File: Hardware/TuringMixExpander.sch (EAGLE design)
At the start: 35 parts, among them IC1 TL074P, IC2 TL072P

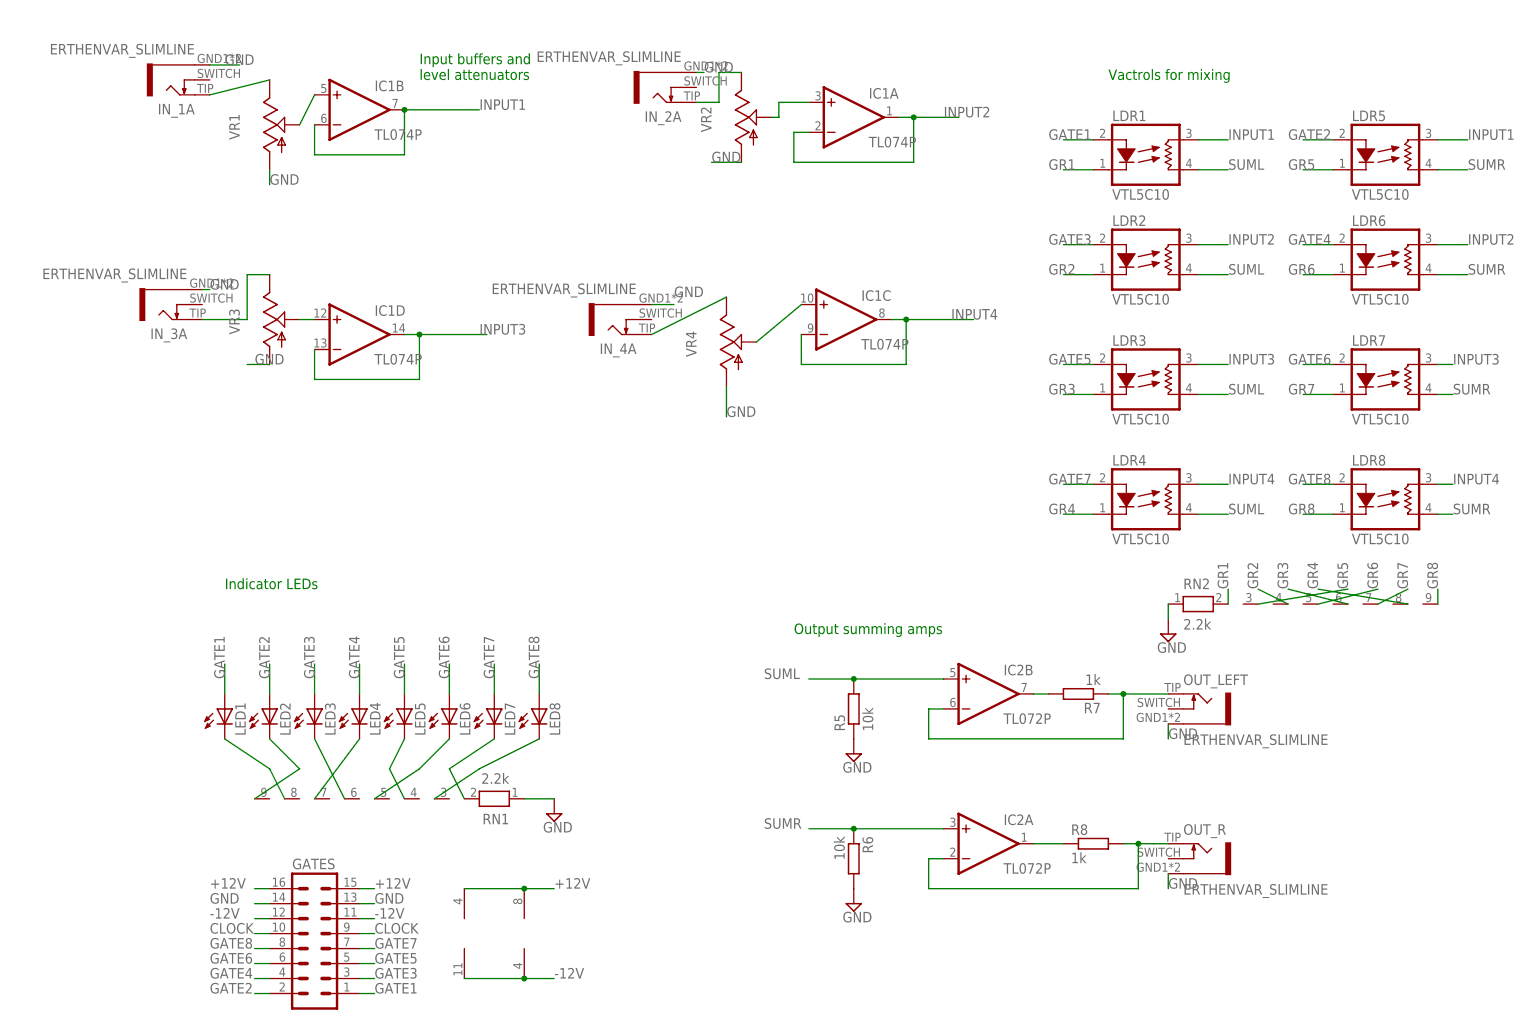
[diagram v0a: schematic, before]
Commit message: New pcb layout
Added passthrough header
Removed resistor networks
Simplified led/resistor structure (one per channel, not two)
New panel layout
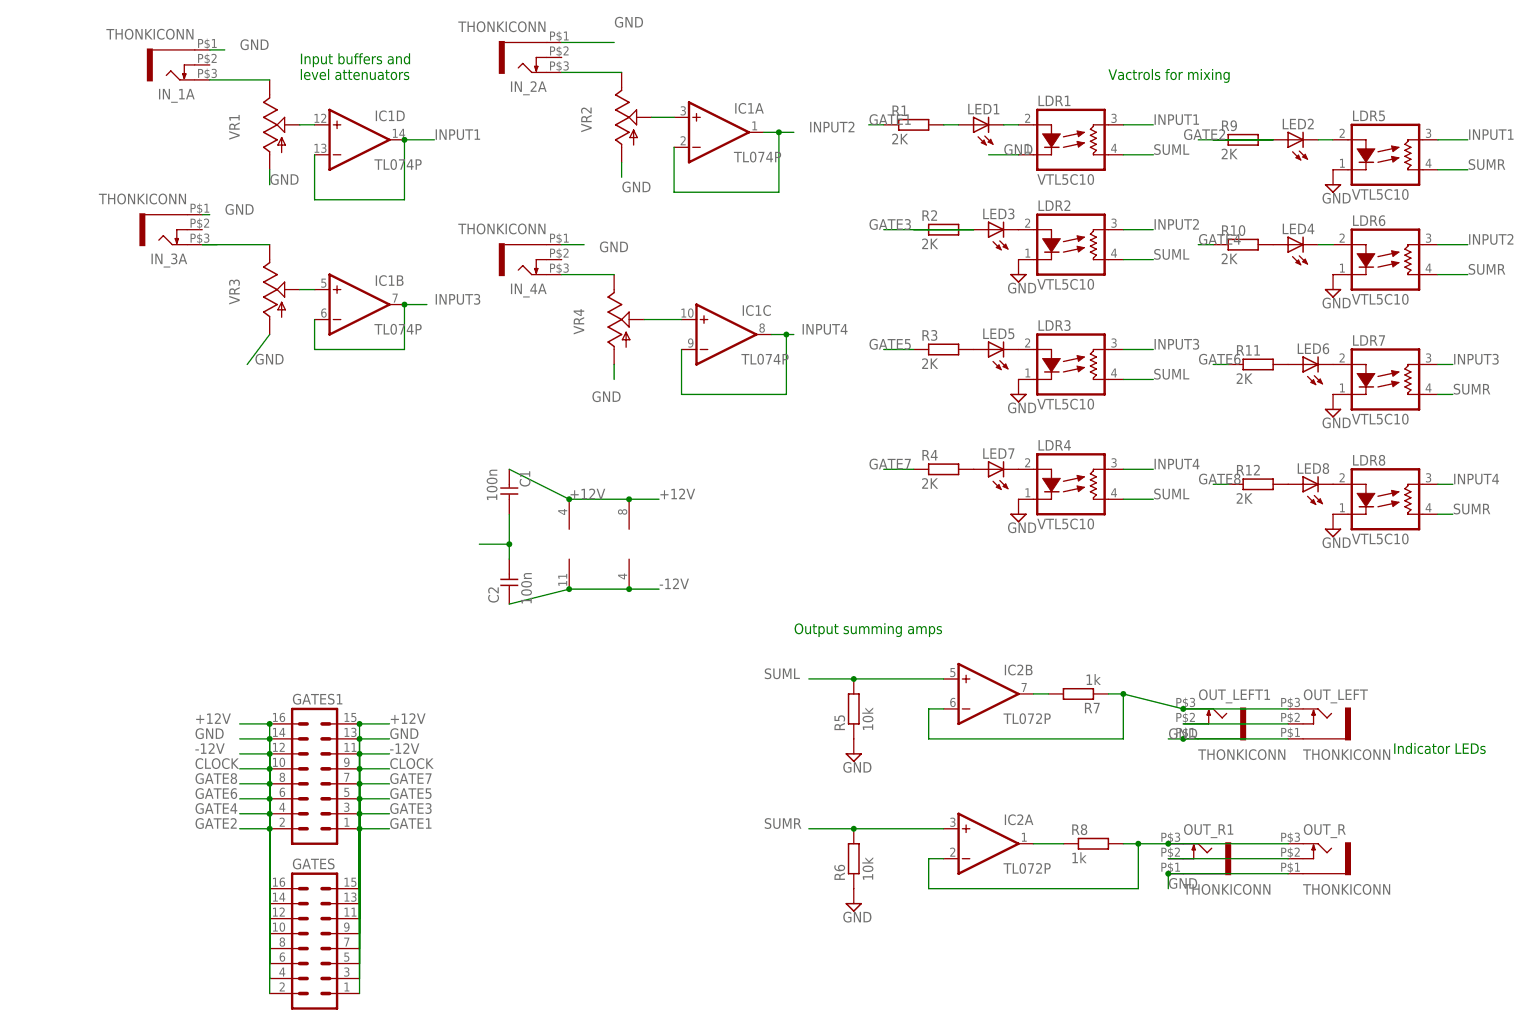
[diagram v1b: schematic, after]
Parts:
- removed RN1, RN2: 2.2k, resistor-net:RN08
- added C1, C2: 100n, TomW:C-EU050-024X044
- added GATES1: (no value), con-lstb:MA08-2
- added OUT_LEFT1, OUT_R1: THONKICONN, TomW:THONKICONN
- added R1, R10, R11, R12, R2, R3, R4, R9: 2K, TomW:R-EU_0207/10
- IN_1A, IN_2A, IN_3A, IN_4A, OUT_LEFT, OUT_R: value ERTHENVAR_SLIMLINE -> THONKICONN; device TomW:ERTHENVAR_SLIMLINE -> TomW:THONKICONN
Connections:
- removed net GR1: LDR1.C, RN2.2
- removed net GR2: LDR2.C, RN2.4
- removed net GR3: LDR3.C, RN2.6
- removed net GR4: LDR4.C, RN2.8
- removed net GR5: LDR5.C, RN2.3
- removed net GR6: LDR6.C, RN2.5
- removed net GR7: LDR7.C, RN2.7
- removed net GR8: LDR8.C, RN2.9
- new net N$14: LDR1.A, LED1.C
- new net N$24: OUT_R.4, OUT_R1.4
- new net N$25: LED1.A, R1.2
- new net N$26: LED3.A, R2.1
- new net N$27: LED5.A, R3.2
- new net N$28: LED7.A, R4.2
- new net N$29: LED2.A, R9.1
- new net N$30: LED4.A, R10.2
- new net N$31: LED6.A, R11.2
- new net N$32: LED8.A, R12.2
- net +12V: now also C1.2, GATES1.15, GATES1.16
- net -12V: now also C2.2, GATES1.11, GATES1.12
- net CLOCK: now also GATES1.10, GATES1.9
- net GATE1: now also GATES1.1, R1.1; no longer LDR1.A, LED1.A
- net GATE2: now also GATES1.2, R9.2; no longer LDR5.A, LED2.A
- net GATE3: now also GATES1.3, R2.2; no longer LDR2.A, LED3.A
- net GATE4: now also GATES1.4, R10.1; no longer LDR6.A, LED4.A
- net GATE5: now also GATES1.5, R3.1; no longer LDR3.A, LED5.A
- net GATE6: now also GATES1.6, R11.1; no longer LDR7.A, LED6.A
- net GATE7: now also GATES1.7, R4.1; no longer LDR4.A, LED7.A
- net GATE8: now also GATES1.8, R12.1; no longer LDR8.A, LED8.A
- net GND: now also C1.1, C2.1, GATES1.13, GATES1.14, LDR1.C, LDR2.C, LDR3.C, LDR4.C, LDR5.C, LDR6.C, LDR7.C, LDR8.C, OUT_LEFT1.5, OUT_R1.5, R6.1; no longer R6.2, RN1.1, RN2.1
- net INPUT1: now also IC1D.-IN, IC1D.OUT; no longer IC1B.-IN, IC1B.OUT
- net INPUT3: now also IC1B.-IN, IC1B.OUT; no longer IC1D.-IN, IC1D.OUT
- net N$10: now also OUT_R1.3
- net N$11: now also IC1B.+IN; no longer IC1D.+IN
- net N$15: now also LDR2.A, LED3.C; no longer LED1.C, RN1.8
- net N$16: now also LDR3.A, LED5.C; no longer LED2.C, RN1.9
- net N$17: now also LDR4.A, LED7.C; no longer LED3.C, RN1.6
- net N$18: now also LDR5.A, LED2.C; no longer LED4.C, RN1.7
- net N$19: now also LDR6.A, LED4.C; no longer LED5.C, RN1.4
- net N$2: now also IC1D.+IN; no longer IC1B.+IN
- net N$20: now also LDR7.A; no longer RN1.5
- net N$21: now also LDR8.A, LED8.C; no longer LED7.C, RN1.2
- net N$22: now also OUT_LEFT.4, OUT_LEFT1.4; no longer LED8.C, RN1.3
- net N$7: now also OUT_LEFT1.3
- net SUMR: now also R6.2; no longer R6.1
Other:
- moved on the sheet: IC1A, IC1B, IC1C, IC1D, IN_1A, IN_2A, IN_3A, IN_4A, LDR1, LDR2, LDR3, LDR4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

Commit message: New resistor grid
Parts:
- R1, R10, R11, R12, R2, R3, R4, R5, R6, R7, R8, R9: device TomW:R-EU_0207/10 -> TomW:R-EU_0207/7
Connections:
- net GATE1: now also R1.2; no longer R1.1
- net GND: now also LDR1.LED-, LDR2.LED-, LDR3.LED-, LDR4.LED-, LDR5.LED-, LDR6.LED-, LDR7.LED-, LDR8.LED-; no longer LDR1.C, LDR2.C, LDR3.C, LDR4.C, LDR5.C, LDR6.C, LDR7.C, LDR8.C
- net INPUT1: now also LDR1.RES1, LDR5.RES1; no longer LDR1.L1, LDR5.L1
- net INPUT2: now also LDR2.RES1, LDR6.RES1; no longer LDR2.L1, LDR6.L1
- net INPUT3: now also LDR3.RES1, LDR7.RES1; no longer LDR3.L1, LDR7.L1
- net INPUT4: now also LDR4.RES1, LDR8.RES1; no longer LDR4.L1, LDR8.L1
- net N$14: now also LDR1.LED+; no longer LDR1.A
- net N$15: now also LDR2.LED+; no longer LDR2.A
- net N$16: now also LDR3.LED+; no longer LDR3.A
- net N$17: now also LDR4.LED+; no longer LDR4.A
- net N$18: now also LDR5.LED+; no longer LDR5.A
- net N$19: now also LDR6.LED+; no longer LDR6.A
- net N$20: now also LDR7.LED+; no longer LDR7.A
- net N$21: now also LDR8.LED+; no longer LDR8.A
- net N$25: now also R1.1; no longer R1.2
- net SUML: now also LDR1.RES2, LDR2.RES2, LDR3.RES2, LDR4.RES2; no longer LDR1.L2, LDR2.L2, LDR3.L2, LDR4.L2
- net SUMR: now also LDR5.RES2, LDR6.RES2, LDR7.RES2, LDR8.RES2; no longer LDR5.L2, LDR6.L2, LDR7.L2, LDR8.L2

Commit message: PCB work
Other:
- moved on the sheet: IN_3A, LED3, R1, R2, R9
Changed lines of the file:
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@@
 <instance part="IN_1A" gate="G$1" x="17.78" y="167.64" rot="R180"/>
 <instance part="IN_2A" gate="G$1" x="77.47" y="168.91" rot="R180"/>
-<instance part="IN_3A" gate="G$1" x="16.51" y="139.7" rot="R180"/>
+<instance part="IN_3A" gate="G$1" x="13.97" y="139.7" rot="R180"/>
 <instance part="IN_4A" gate="G$1" x="77.47" y="134.62" rot="R180"/>
 <instance part="IC1" gate="D" x="48.26" y="154.94"/>
@@
 <instance part="LED1" gate="G$1" x="152.4" y="157.48" rot="R90"/>
 <instance part="LED2" gate="G$1" x="205.74" y="154.94" rot="R90"/>
-<instance part="LED3" gate="G$1" x="154.94" y="139.7" rot="R90"/>
+<instance part="LED3" gate="G$1" x="152.4" y="139.7" rot="R90"/>
 <instance part="LED4" gate="G$1" x="205.74" y="137.16" rot="R90"/>
 <instance part="LED5" gate="G$1" x="154.94" y="119.38" rot="R90"/>
@@
 <instance part="FRAME1" gate="G$1" x="0" y="0"/>
 <instance part="GATES1" gate="G$1" x="40.64" y="45.72"/>
-<instance part="R1" gate="G$1" x="142.24" y="157.48"/>
+<instance part="R1" gate="G$1" x="142.24" y="157.48" rot="R180"/>
 <instance part="C1" gate="G$1" x="73.66" y="93.98" rot="R180"/>
 <instance part="C2" gate="G$1" x="73.66" y="81.28"/>
@@
 <instance part="SUPPLY8" gate="GND" x="213.36" y="129.54"/>
 <instance part="SUPPLY9" gate="GND" x="213.36" y="147.32"/>
-<instance part="R2" gate="G$1" x="147.32" y="139.7"/>
+<instance part="R2" gate="G$1" x="142.24" y="139.7" rot="R180"/>
 <instance part="R3" gate="G$1" x="147.32" y="119.38"/>
 <instance part="R4" gate="G$1" x="147.32" y="99.06"/>
-<instance part="R9" gate="G$1" x="198.12" y="154.94"/>
+<instance part="R9" gate="G$1" x="198.12" y="154.94" rot="R180"/>
 <instance part="R10" gate="G$1" x="198.12" y="137.16"/>
 <instance part="R11" gate="G$1" x="200.66" y="116.84"/>
@@
 <segment>
 <pinref part="IN_3A" gate="G$1" pin="5"/>
-<wire x1="22.86" y1="142.24" x2="21.59" y2="142.24" width="0.1524" layer="91"/>
+<wire x1="22.86" y1="142.24" x2="19.05" y2="142.24" width="0.1524" layer="91"/>
 <label x="25.4" y="142.24" size="1.778" layer="95"/>
 </segment>
@@
 <wire x1="68.58" y1="86.36" x2="73.66" y2="86.36" width="0.1524" layer="91"/>
 <junction x="73.66" y="86.36"/>
+<label x="66.04" y="86.36" size="1.778" layer="95" rot="R180"/>
 </segment>
 <segment>
@@
 <segment>
 <pinref part="R1" gate="G$1" pin="2"/>
-<wire x1="134.62" y1="157.48" x2="147.32" y2="157.48" width="0.1524" layer="91"/>
+<wire x1="134.62" y1="157.48" x2="137.16" y2="157.48" width="0.1524" layer="91"/>
 <label x="134.62" y="157.48" size="1.778" layer="95"/>
 </segment>
@@
 <segment>
 <pinref part="R9" gate="G$1" pin="2"/>
-<wire x1="190.5" y1="154.94" x2="203.2" y2="154.94" width="0.1524" layer="91"/>
+<wire x1="190.5" y1="154.94" x2="193.04" y2="154.94" width="0.1524" layer="91"/>
 <label x="187.96" y="154.94" size="1.778" layer="95"/>
 </segment>
@@
 <segment>
 <pinref part="R2" gate="G$1" pin="2"/>
-<wire x1="137.16" y1="139.7" x2="152.4" y2="139.7" width="0.1524" layer="91"/>
+<wire x1="134.62" y1="139.7" x2="137.16" y2="139.7" width="0.1524" layer="91"/>
 <label x="134.62" y="139.7" size="1.778" layer="95"/>
 </segment>
@@
 <segment>
 <pinref part="VR3" gate="G$1" pin="E"/>
-<wire x1="33.02" y1="137.16" x2="21.59" y2="137.16" width="0.1524" layer="91"/>
+<wire x1="33.02" y1="137.16" x2="19.05" y2="137.16" width="0.1524" layer="91"/>
 <pinref part="IN_3A" gate="G$1" pin="3"/>
-<wire x1="24.13" y1="137.16" x2="21.59" y2="137.16" width="0.1524" layer="91"/>
 </segment>
 </net>
@@
 <pinref part="LDR2" gate="G$1" pin="LED+"/>
 <pinref part="LED3" gate="G$1" pin="C"/>
+<wire x1="157.48" y1="139.7" x2="160.02" y2="139.7" width="0.1524" layer="91"/>
 </segment>
 </net>
@@
 <pinref part="LED1" gate="G$1" pin="A"/>
 <pinref part="R1" gate="G$1" pin="1"/>
-<wire x1="137.16" y1="157.48" x2="149.86" y2="157.48" width="0.1524" layer="91"/>
+<wire x1="147.32" y1="157.48" x2="149.86" y2="157.48" width="0.1524" layer="91"/>
 </segment>
 </net>
@@
 <pinref part="LED3" gate="G$1" pin="A"/>
 <pinref part="R2" gate="G$1" pin="1"/>
-<wire x1="152.4" y1="139.7" x2="142.24" y2="139.7" width="0.1524" layer="91"/>
+<wire x1="147.32" y1="139.7" x2="149.86" y2="139.7" width="0.1524" layer="91"/>
 </segment>
 </net>
@@
 <pinref part="LED2" gate="G$1" pin="A"/>
 <pinref part="R9" gate="G$1" pin="1"/>
-<wire x1="203.2" y1="154.94" x2="193.04" y2="154.94" width="0.1524" layer="91"/>
 </segment>
 </net>
@@
 </sheet>
 </sheets>
+<errors>
+</errors>
 </schematic>
 </drawing>
